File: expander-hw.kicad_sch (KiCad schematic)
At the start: 29 parts, among them J1 Conn_ARM_SWD_TagConnect_TC203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, J2 USB_C_Receptacle_USB2.0_16P, J3 Conn_02x08_Odd_Even, U1 STM32H523RETx, U2 USBLC6-2SC6, U3 AZ1117-3.3, U4 SRDA3.3-4BTG, U5 SRDA3.3-4BTG, U6 SRDA3.3-4BTG

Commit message: Add DAC hardware
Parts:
- removed J3: Conn_02x08_Odd_Even, Connector_PinHeader_2.54mm:PinHeader_2x08_P2.54mm_Vertical, symbol Connector_Generic:Conn_02x08_Odd_Even
- added C12: 6.8pF, Capacitor_SMD:C_0603_1608Metric, symbol Device:C
- added C13: 7.5pF, Capacitor_SMD:C_0603_1608Metric, symbol Device:C
- added C14, C15: 22uF, Capacitor_SMD:C_0805_2012Metric, symbol Device:C
- added C16: 10uF, Capacitor_SMD:C_0603_1608Metric, symbol Device:C
- added C17, C3: 100nF, Capacitor_SMD:C_0603_1608Metric, symbol Device:C
- added C18: 10nF, Capacitor_SMD:C_0603_1608Metric, symbol Device:C
- added C19: 4.7nF, Capacitor_SMD:C_0603_1608Metric, symbol Device:C
- added C20: 220nF, Capacitor_SMD:C_0603_1608Metric, symbol Device:C
- added D2, D3: D_Schottky, Diode_SMD:D_1206_3216Metric_Pad1.42x1.75mm_HandSolder, symbol Device:D_Schottky
- added J2: Conn_02x10_Odd_Even, Connector_PinHeader_2.54mm:PinHeader_2x10_P2.54mm_Horizontal, symbol Connector_Generic:Conn_02x10_Odd_Even
- added L1, L2: 4.7uH, Inductor_SMD:L_1210_3225Metric, symbol Device:L
- added NT1, NT2: NetTie_2, NetTie:NetTie-2_SMD_Pad0.5mm, symbol Device:NetTie_2
- added R1, R12, R18, R21, R4, R5: 100k, Resistor_SMD:R_0603_1608Metric, symbol Device:R
- added R17: 900k, Resistor_SMD:R_0603_1608Metric, symbol Device:R
- added R19: 1M, Resistor_SMD:R_0603_1608Metric, symbol Device:R
- added R2, R3, R6, R7: 10k, Resistor_SMD:R_0603_1608Metric, symbol Device:R
- added R20: 100, Resistor_SMD:R_0603_1608Metric, symbol Device:R
- added U2: OPA2994xD, Package_SO:SOIC-8_3.9x4.9mm_P1.27mm, symbol Amplifier_Operational:OPA2994xD
- added U3: DAC8562, Package_SO:VSSOP-10_3x3mm_P0.5mm, symbol expander-hw:DAC8562
- added U9: TPS65130RGE, Package_DFN_QFN:VQFN-24-1EP_4x4mm_P0.5mm_EP2.45x2.45mm_ThermalVias, symbol Regulator_Switching:TPS65130RGE
- C2: value 10uF -> 150nF; footprint Capacitor_SMD:C_0805_2012Metric -> Capacitor_SMD:C_0603_1608Metric
- TP1: footprint TestPoint:TestPoint_Pad_D1.0mm -> TestPoint:TestPoint_Pad_D2.5mm
- renumbered C8 to C1, C6 to C10, C7 to C11, C9 to C4, C10 to C5, C1 to C6, C3 to C7, C4 to C8, C5 to C9, J2 to J3, R5 to R10, R6 to R11, R2 to R13, R1 to R14, R7 to R15, R8 to R16, R3 to R8, R4 to R9, U4 to U1, U5 to U4, U1 to U5, U2 to U6, U6 to U7, U3 to U8
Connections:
- net HW_V0 is gone; now on net +3.3V: U5.33 (PB12)
- net +3.3V: now also J2.5 (Pin_5), U3.9 (AV_{DD}); no longer C2.1
- net GND: now also C14.2, C15.2, C16.2, C17.2, C18.2, C19.2, C20.2, J2.15 (Pin_15), J2.16 (Pin_16), L2.2, NT1.1, NT2.1, R18.1, U9.19 (AGND), U9.2 (PGND), U9.25 (EP), U9.3 (PGND); no longer C2.2
- net I2C1_SCL: now also J2.20 (Pin_20)
- net I2C1_SDA: now also J2.19 (Pin_19)
- net I2C3_SCL: now also J2.18 (Pin_18)
- net I2C3_SDA: now also J2.17 (Pin_17)
- net SPI1_CS: now also J2.10 (Pin_10)
- net SPI1_MISO: now also J2.8 (Pin_8)
- net SPI1_MOSI: now also J2.9 (Pin_9)
- net SPI1_SCK: now also J2.7 (Pin_7)
- net SPI4_CS: now also J2.14 (Pin_14)
- net SPI4_MISO: now also J2.12 (Pin_12)
- net SPI4_MOSI: now also J2.13 (Pin_13)
- net SPI4_SCK: now also J2.11 (Pin_11)
- net VBUS: now also C16.1, J2.6 (Pin_6), L1.1, R20.2, U9.5 (INN), U9.6 (INN)
- net DAC_DIN: now reaches U5.17 (PA3)
- net DAC_DIN: now also U3.8 (D_{IN})
- net DAC_SYNC: now reaches U5.20 (PA4)
- net DAC_SYNC: now also U3.6 (~{SYNC})
- net DAC_LOAD: now reaches U5.26 (PB0)
- net DAC_LOAD: now also U3.4 (~{LDAC})
- net DAC_CLK: now reaches U5.27 (PB1)
- net DAC_CLK: now also U3.7 (SCLK)
- new net: C20.1, R21.1, U9.17 (VREF)
- new net: C13.2, R19.1, R21.2, U9.16 (FBN)
- new net: C17.1, R20.1, U9.10 (ENN), U9.11 (PSN), U9.4 (VIN), U9.8 (ENP), U9.9 (PSP)
- new net: R3.1, R4.2, U2.5 (+)
- new net: R5.2, R6.1, U2.2 (-)
- new net: C2.1, R2.2, R6.2, U3.10 (V_{REF}IN/OUT)
- new net: R1.2, R2.1, U2.6 (-)
- new net: R12.2, R7.1, U2.3 (+)
- new net: R7.2, U3.2 (V_{OUT}B)
- new net: C12.2, R17.1, R18.2, U9.22 (FBP)
- new net: R3.2, U3.1 (V_{OUT}A)
- new net: C19.1, U9.18 (CN)
- new net: C18.1, U9.21 (CP)
- new net +12V: C12.1, C14.1, C3.1, D2.1 (K), R17.2, U2.8 (V+), U9.23 (VPOS)
- new net -12V: C13.1, C15.1, C3.2, D3.2 (A), R19.2, U2.4 (V-), U9.15 (VNEG)
- new net A0: J2.1 (Pin_1), R1.1, U2.7
- new net A1: J2.2 (Pin_2), R5.1, U2.1
- new net CoilNeg: D3.1 (K), L2.1, U9.13 (OUTN), U9.14 (OUTN)
- new net CoilPos: D2.2 (A), L1.2, U9.1 (INP), U9.24 (INP)
- new net DAC_CLR: U3.5 (~{CLR})
- new net GNDA: C2.2, J2.3 (Pin_3), J2.4 (Pin_4), NT1.2, NT2.2, R12.1, R4.1, U3.3 (GND)
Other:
- moved on the sheet: C10, C11, C7, C8, C9

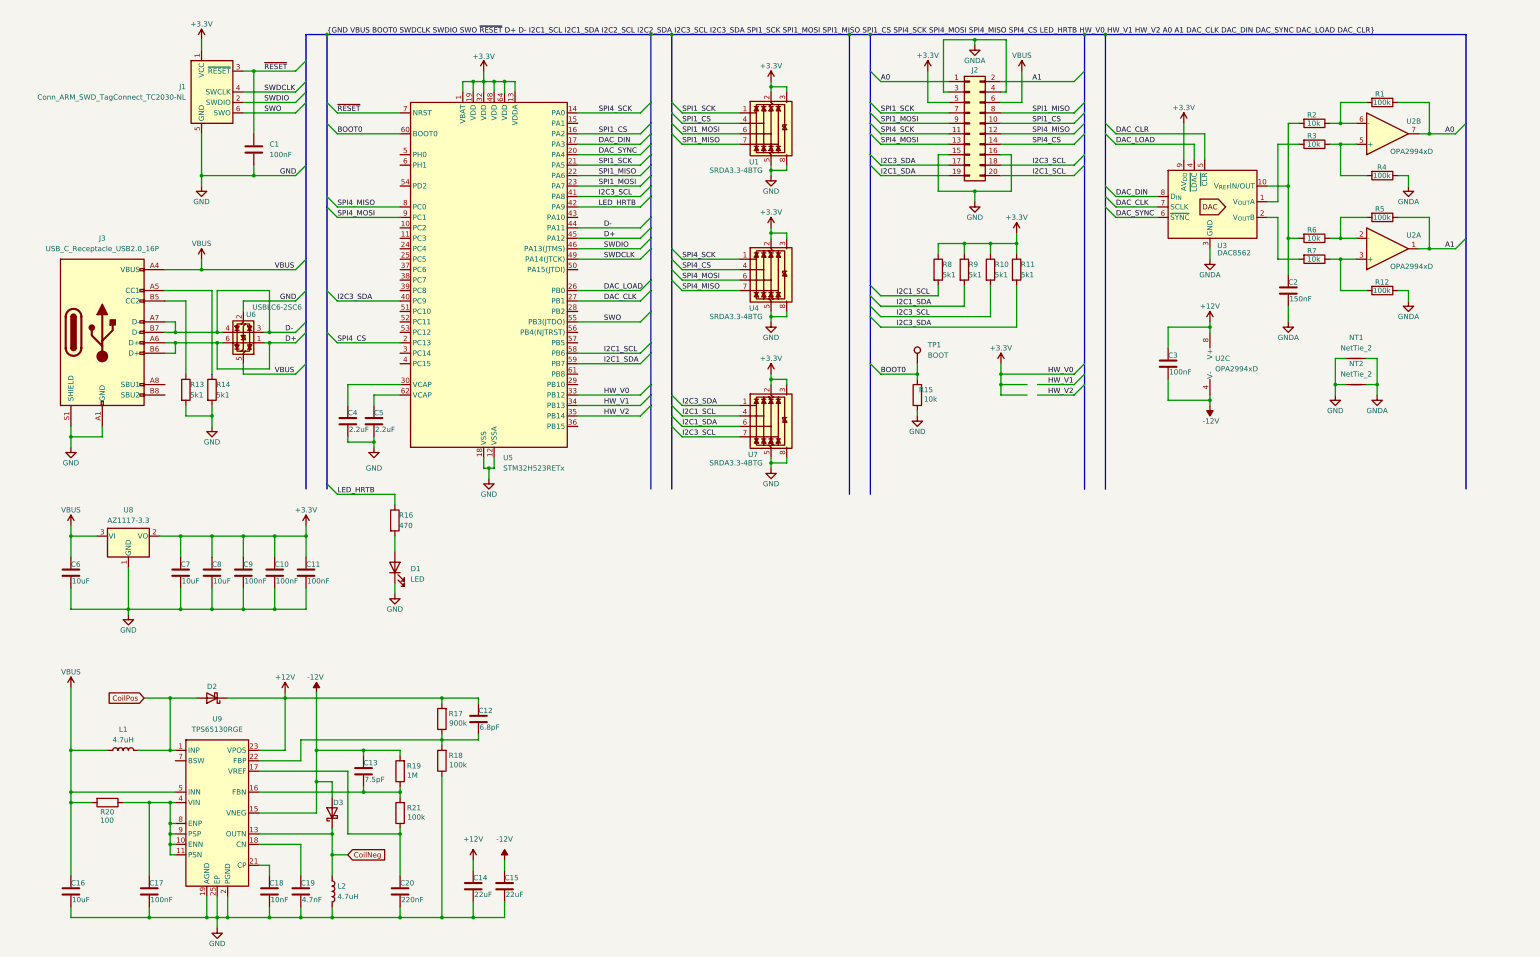
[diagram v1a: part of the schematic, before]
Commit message: Fix boost converter + vref
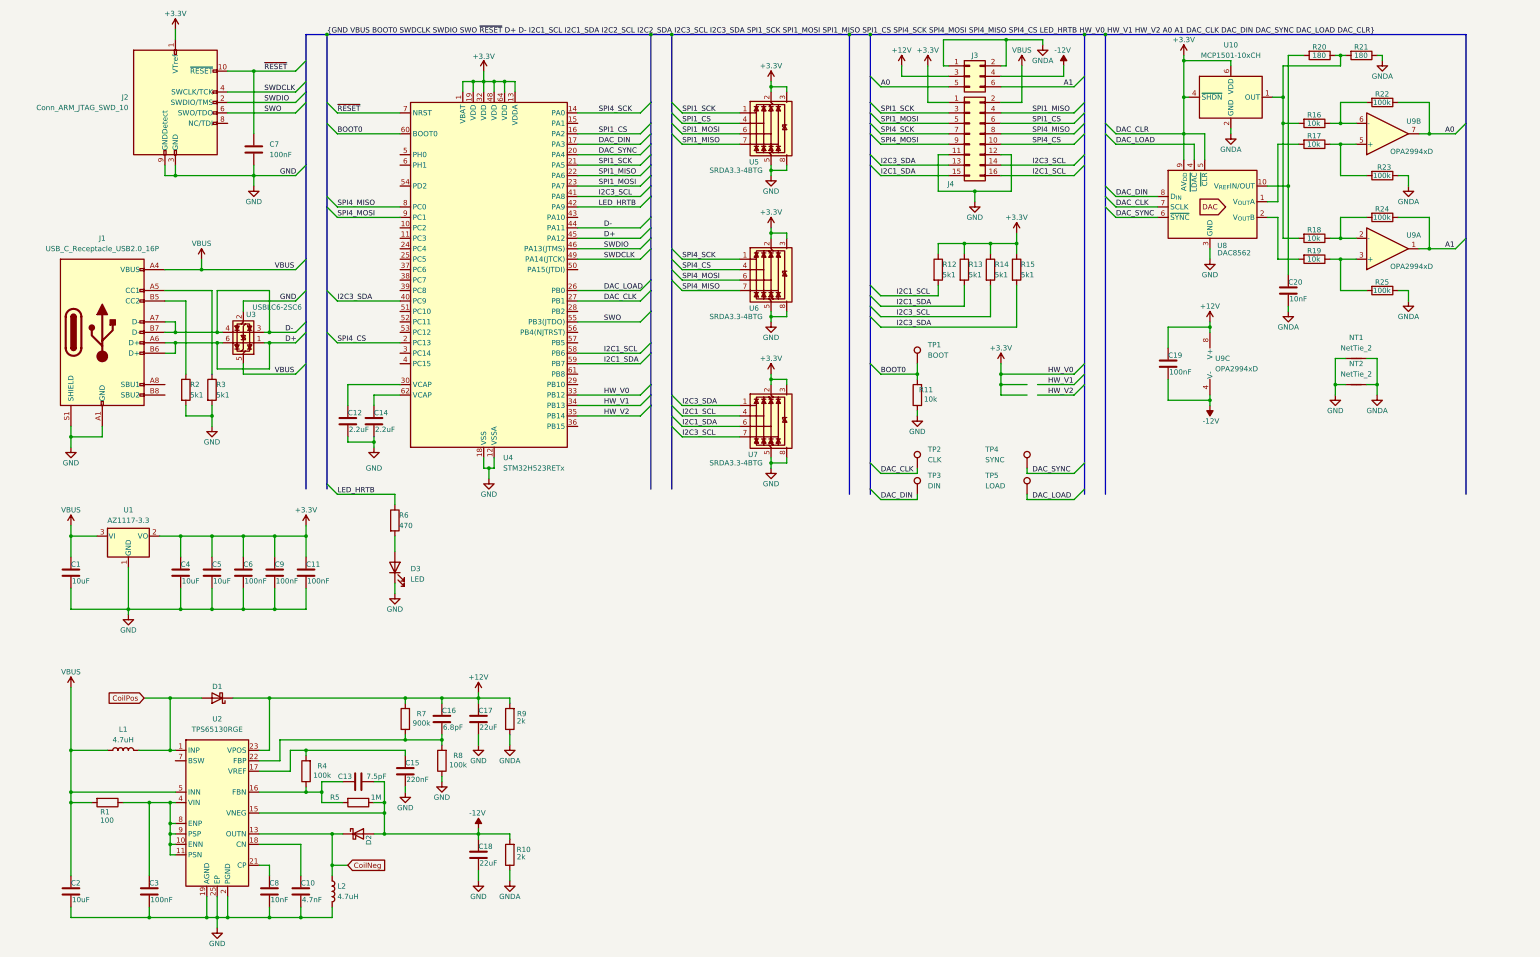
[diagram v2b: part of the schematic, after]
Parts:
- removed J1: Conn_ARM_SWD_TagConnect_TC2030-NL, Connector:Tag-Connect_TC2030-IDC-NL_2x03_P1.27mm_Vertical, symbol Connector:Conn_ARM_SWD_TagConnect_TC2030-NL
- removed J2: Conn_02x10_Odd_Even, Connector_PinHeader_2.54mm:PinHeader_2x10_P2.54mm_Horizontal, symbol Connector_Generic:Conn_02x10_Odd_Even
- added J2: Conn_ARM_JTAG_SWD_10, Connector_PinHeader_1.27mm:PinHeader_2x05_P1.27mm_Vertical, symbol Connector:Conn_ARM_JTAG_SWD_10
- added J3: Conn_02x03_Odd_Even, Connector_PinHeader_2.54mm:PinHeader_2x03_P2.54mm_Horizontal, symbol Connector_Generic:Conn_02x03_Odd_Even
- added J4: Conn_02x08_Odd_Even, Connector_PinHeader_2.54mm:PinHeader_2x08_P2.54mm_Horizontal, symbol Connector_Generic:Conn_02x08_Odd_Even
- added R10, R9: 2k, Resistor_SMD:R_0805_2012Metric, symbol Device:R
- added R20, R21: 180, Resistor_SMD:R_0603_1608Metric, symbol Device:R
- added TP2: CLK, TestPoint:TestPoint_Pad_D1.0mm, symbol Connector:TestPoint
- added TP3: DIN, TestPoint:TestPoint_Pad_D1.0mm, symbol Connector:TestPoint
- added TP4: SYNC, TestPoint:TestPoint_Pad_D1.0mm, symbol Connector:TestPoint
- added TP5: LOAD, TestPoint:TestPoint_Pad_D1.0mm, symbol Connector:TestPoint
- added U10: MCP1501-10xCH, Package_TO_SOT_SMD:SOT-23-6, symbol Reference_Voltage:MCP1501-10xCH
- C20: renamed from C2; value 150nF -> 10nF
- renumbered C6 to C1, C19 to C10, C4 to C12, C5 to C14, C20 to C15, C12 to C16, C14 to C17, C15 to C18, C3 to C19, C16 to C2, C17 to C3, C7 to C4, C8 to C5, C9 to C6, C1 to C7, C18 to C8, C10 to C9, D2 to D1, D3 to D2, D1 to D3, J3 to J1, R20 to R1, R15 to R11, R8 to R12, R9 to R13, R10 to R14, R11 to R15, R2 to R16, R3 to R17, R6 to R18, R7 to R19, R13 to R2, R1 to R22, R4 to R23, R5 to R24, R12 to R25, R14 to R3, R21 to R4, R19 to R5, R16 to R6, R17 to R7, R18 to R8, U8 to U1, U9 to U2, U6 to U3, U5 to U4, U1 to U5, U4 to U6, U3 to U8, U2 to U9
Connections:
- net DAC_CLR is gone; now on net +3.3V: U8.5 (~{CLR})
- net +12V: now also J3.3 (Pin_3), R9.2
- net +3.3V: now also J2.1 (VTref), J4.1 (Pin_1), U10.4 (~{SHDN}), U10.6 (VDD)
- net -12V: now also C13.2, R5.1, J3.4 (Pin_4), R10.2; no longer C13.1, R5.2
- net A0: now also J3.5 (Pin_5)
- net A1: now also J3.6 (Pin_6)
- net DAC_CLK: now also TP2.1
- net DAC_DIN: now also TP3.1
- net DAC_LOAD: now also TP5.1
- net DAC_SYNC: now also TP4.1
- net GND: now also U8.3 (GND), J2.3 (GND), J2.5 (GND), J2.9 (GNDDetect), J4.11 (Pin_11), J4.12 (Pin_12)
- net GNDA: now also J3.1 (Pin_1), J3.2 (Pin_2), R10.1, R21.1, R9.1, U10.2 (GND), U10.3 (GND), U10.5 (GND); no longer U8.3 (GND)
- net I2C1_SCL: now also J4.16 (Pin_16)
- net I2C1_SDA: now also J4.15 (Pin_15)
- net I2C3_SCL: now also J4.14 (Pin_14)
- net I2C3_SDA: now also J4.13 (Pin_13)
- net SPI1_CS: now also J4.6 (Pin_6)
- net SPI1_MISO: now also J4.4 (Pin_4)
- net SPI1_MOSI: now also J4.5 (Pin_5)
- net SPI1_SCK: now also J4.3 (Pin_3)
- net SPI4_CS: now also J4.10 (Pin_10)
- net SPI4_MISO: now also J4.8 (Pin_8)
- net SPI4_MOSI: now also J4.9 (Pin_9)
- net SPI4_SCK: now also J4.7 (Pin_7)
- net SWDCLK: now also J2.4 (SWCLK/TCK)
- net SWDIO: now also J2.2 (SWDIO/TMS)
- net SWO: now also J2.6 (SWO/TDO)
- net VBUS: now also J4.2 (Pin_2)
- net ~{RESET}: now also J2.10 (~{RESET})
- net at C15.1, U2.17 (VREF): now also R4.2; no longer R4.1
- net at R16.2, R18.2: now also R20.1, R21.2, U10.1 (OUT); no longer C20.1, U8.10 (V_{REF}IN/OUT)
- new net: C13.1, R4.1, R5.2, U2.16 (FBN)
- new net: C20.1, R20.2, U8.10 (V_{REF}IN/OUT)
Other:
- moved on the sheet: C13, C15, C16, C17, C18, D1, D2, R4, R5, R7

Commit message: Refactor dac gain
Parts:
- removed TP2: CLK, TestPoint:TestPoint_Pad_D1.0mm, symbol Connector:TestPoint
- removed TP3: DIN, TestPoint:TestPoint_Pad_D1.0mm, symbol Connector:TestPoint
- removed TP4: SYNC, TestPoint:TestPoint_Pad_D1.0mm, symbol Connector:TestPoint
- removed TP5: LOAD, TestPoint:TestPoint_Pad_D1.0mm, symbol Connector:TestPoint
- added C21: 100nF, Capacitor_SMD:C_0603_1608Metric, symbol Device:C
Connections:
- net +3.3V: now also C21.1
- net GND: now also C21.2

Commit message: Small aesthetic changes
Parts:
- C19: value 100nF -> 1uF
- R16, R17, R18, R19: value 10k -> 47k
- R22, R23, R24, R25: value 100k -> 470k
- R5: value 1M -> 1.1M
- R7: value 900k -> 1M
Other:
- moved on the sheet: R5
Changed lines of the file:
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@@
 	(wire
 		(pts
-			(xy 96.52 209.55) (xy 99.06 209.55)
+			(xy 95.25 209.55) (xy 99.06 209.55)
 		)
 		(stroke
@@
 	(wire
 		(pts
-			(xy 83.82 209.55) (xy 88.9 209.55)
+			(xy 83.82 209.55) (xy 87.63 209.55)
 		)
 		(stroke
@@
 		(dnp no)
 		(property "Reference" "R4"
-			(at 85.09 200.66 0)
+			(at 84.074 200.66 0)
 			(effects
 				(font
@@
 			)
 		)
-		(property "Value" "100k"
+		(property "Value" "470k"
 			(at 339.344 57.15 90)
 			(effects
@@
 			)
 		)
-		(property "Value" "100k"
+		(property "Value" "470k"
 			(at 339.344 67.31 90)
 			(effects
@@
 		(dnp no)
 		(property "Reference" "D2"
-			(at 95.25 217.424 90)
+			(at 93.98 214.63 0)
 			(effects
 				(font
@@
 			)
 		)
-		(property "Value" "10k"
+		(property "Value" "47k"
 			(at 323.342 72.39 90)
 			(effects
@@
 		)
 		(property "Value" "2k"
-			(at 133.35 189.738 0)
+			(at 133.35 189.992 0)
 			(effects
 				(font
@@
 			)
 		)
-		(property "Value" "10k"
+		(property "Value" "47k"
 			(at 323.342 44.45 90)
 			(effects
@@
 			)
 		)
-		(property "Value" "10k"
+		(property "Value" "47k"
 			(at 323.342 77.47 90)
 			(effects
@@
 	(symbol
 		(lib_id "Device:R")
-		(at 92.71 209.55 270)
+		(at 91.44 209.55 270)
 		(unit 1)
 		(exclude_from_sim no)
@@
 		(dnp no)
 		(property "Reference" "R5"
-			(at 85.852 208.28 90)
+			(at 85.598 208.28 90)
 			(effects
 				(font
@@
 			)
 		)
-		(property "Value" "1M"
-			(at 95.758 208.28 90)
+		(property "Value" "1.1M"
+			(at 94.234 208.28 90)
 			(effects
 				(font
@@
 		)
 		(property "Footprint" "Resistor_SMD:R_0603_1608Metric"
-			(at 92.71 207.772 90)
+			(at 91.44 207.772 90)
 			(effects
 				(font
@@
 		)
 		(property "Datasheet" "~"
-			(at 92.71 209.55 0)
+			(at 91.44 209.55 0)
 			(effects
 				(font
@@
 		)
 		(property "Description" "Resistor"
-			(at 92.71 209.55 0)
+			(at 91.44 209.55 0)
 			(effects
 				(font
@@
 			)
 		)
-		(property "Value" "100k"
+		(property "Value" "470k"
 			(at 339.344 39.37 90)
 			(effects
@@
 		)
 		(property "Value" "2k"
-			(at 133.35 222.758 0)
+			(at 133.35 223.012 0)
 			(effects
 				(font
@@
 		(dnp no)
 		(property "Reference" "R8"
-			(at 118.11 198.12 0)
+			(at 117.094 198.374 0)
 			(effects
 				(font
@@
 			)
 		)
-		(property "Value" "10k"
+		(property "Value" "47k"
 			(at 323.342 49.53 90)
 			(effects
@@
 			)
 		)
-		(property "Value" "100nF"
+		(property "Value" "1uF"
 			(at 289.814 104.902 0)
 			(effects
@@
 			)
 		)
-		(property "Value" "100k"
+		(property "Value" "470k"
 			(at 339.344 85.09 90)
 			(effects
@@
 		(dnp no)
 		(property "Reference" "R7"
-			(at 109.22 187.96 0)
+			(at 108.458 188.214 0)
 			(effects
 				(font
@@
 			)
 		)
-		(property "Value" "900k"
-			(at 110.236 190.246 0)
+		(property "Value" "1M"
+			(at 108.458 190.246 0)
 			(effects
 				(font

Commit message: Minor refactoring
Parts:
- removed C5: 10uF, Capacitor_SMD:C_0805_2012Metric, symbol Device:C
- C2: footprint Capacitor_SMD:C_0603_1608Metric -> Capacitor_SMD:C_0805_2012Metric
- C4: value 10uF -> 22uF
- D1, D2: footprint Diode_SMD:D_1206_3216Metric_Pad1.42x1.75mm_HandSolder -> Diode_SMD:D_1206_3216Metric
- R12, R13, R14, R15: value 5k1 -> 560
- renumbered C21 to C11, C6 to C5, C9 to C6, C11 to C9
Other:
- moved on the sheet: C11, C2, C3, C5, C6, C9
